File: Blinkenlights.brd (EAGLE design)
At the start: 33 x 44.5 mm, 15 parts, among them Q1 2N2222, Q2 2N2222

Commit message: 2.0.0913 Version updates
Minor modifications and tweaking
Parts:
- +, -: device adafruit:1X01 -> IXR:1X01-CLEANBIG
- Q1, Q2: device adafruit:TO92-EBC-OVAL -> IXR:TO92-EBC-OVAL
- U$1: device SparkFun:OSHW-LOGO-S -> IXR:OSHW-LOGO-S
- moved U$1 6.63 mm to (23.5, 36.2)
- moved LED2 1.42 mm to (26.7, 39.4)
- moved LED1 1.42 mm to (6.35, 39.4)
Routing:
- net N$6: track 14.9 -> 13.8 mm
- net N$5: track 14.9 -> 13.8 mm
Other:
- board text added: "BLINKENLIGHTS V2.0.0913"
- board text added: "CR2032 3V"
- board text added: "I LEARNED TO SOLDER!"
- board text removed: "BLINKENLIGHTS V2.0.0613"
- board text removed: "I Learned To Solder!"

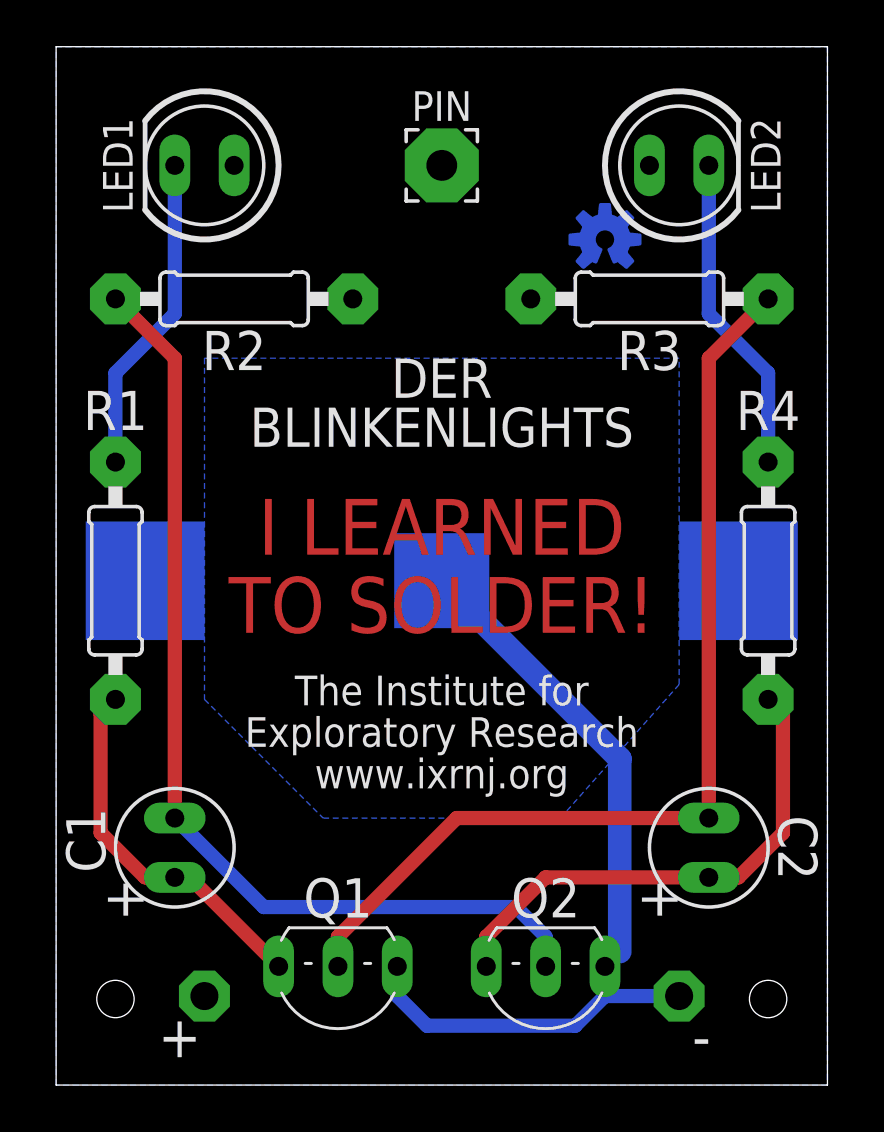
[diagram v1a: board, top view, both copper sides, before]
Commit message: v2.0.1401 Flipped battery clip - could not insert battery when lapel pin was installed.
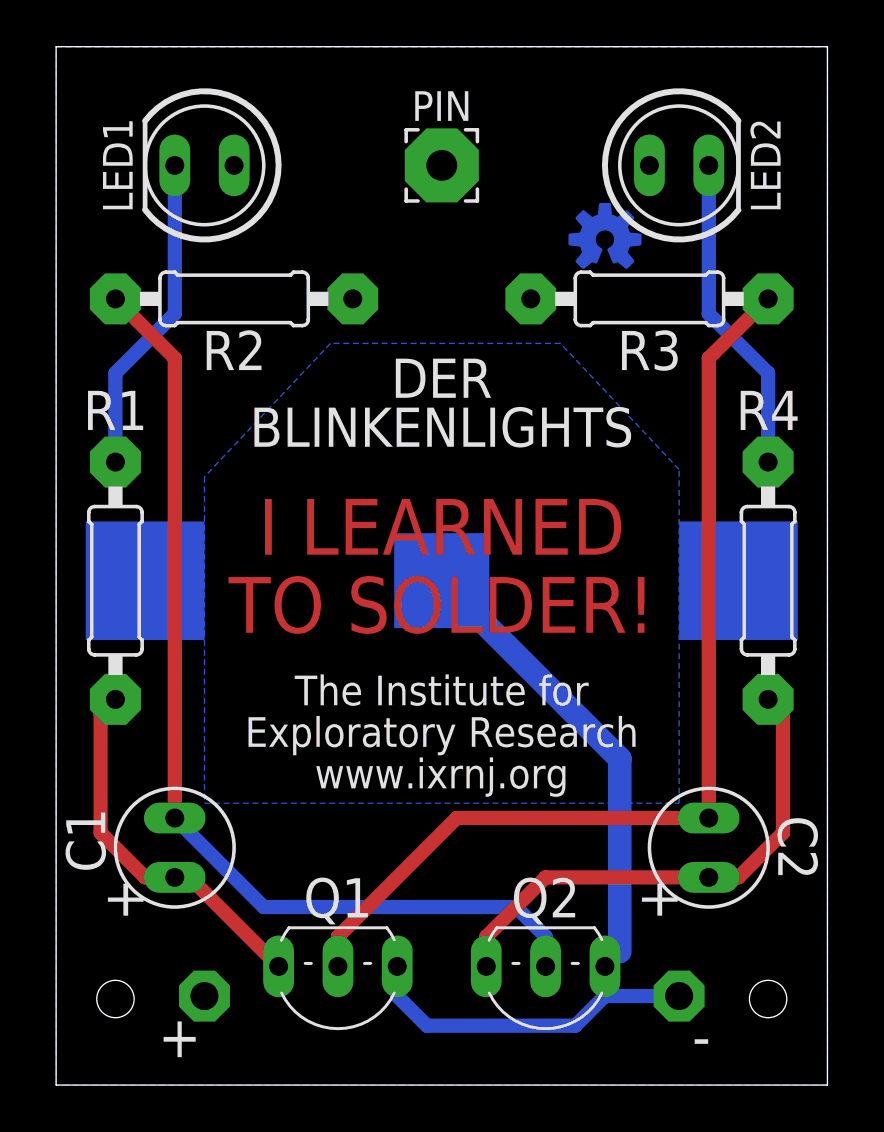
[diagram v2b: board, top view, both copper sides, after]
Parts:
- turned BATT to 180 degrees
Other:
- board text added: "BLINKENLIGHTS V2.0.1401"
- board text removed: "BLINKENLIGHTS V2.0.0913"
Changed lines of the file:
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@@
 <setting verticaltext="up"/>
 </settings>
-<grid distance="0.05" unitdist="inch" unit="inch" style="lines" multiple="1" display="yes" altdistance="0.0125" altunitdist="inch" altunit="inch"/>
+<grid distance="0.05" unitdist="inch" unit="inch" style="lines" multiple="1" display="yes" altdistance="0.0025" altunitdist="inch" altunit="inch"/>
 <layers>
 <layer number="1" name="Top" color="4" fill="1" visible="yes" active="yes"/>
@@
 <layer number="27" name="tValues" color="7" fill="1" visible="yes" active="yes"/>
 <layer number="28" name="bValues" color="7" fill="1" visible="no" active="yes"/>
-<layer number="29" name="tStop" color="7" fill="3" visible="yes" active="yes"/>
+<layer number="29" name="tStop" color="7" fill="3" visible="no" active="yes"/>
 <layer number="30" name="bStop" color="7" fill="6" visible="no" active="yes"/>
 <layer number="31" name="tCream" color="7" fill="4" visible="no" active="yes"/>
@@
 <hole x="2.54" y="3.683" drill="1.6"/>
 <hole x="30.48" y="3.683" drill="1.6"/>
-<text x="16.51" y="1.27" size="1.27" layer="26" font="vector" ratio="12" distance="0" rot="MR0" align="center">BLINKENLIGHTS V2.0.0913</text>
+<text x="16.51" y="1.27" size="1.27" layer="26" font="vector" ratio="12" distance="0" rot="MR0" align="center">BLINKENLIGHTS V2.0.1401</text>
 <text x="16.51" y="22.225" size="2.3876" layer="1" font="vector" ratio="18" distance="40" align="center">I LEARNED
 TO SOLDER!</text>
@@
 BLINKENLIGHTS</text>
 <text x="14.605" y="36.195" size="1.4224" layer="22" font="vector" ratio="12" rot="MR0" align="center">(CC) BY-SA</text>
-<text x="16.51" y="10.16" size="1.778" layer="22" font="vector" ratio="12" distance="0" rot="MR0" align="center">CR2032 3V</text>
+<text x="16.51" y="8.5725" size="1.778" layer="22" font="vector" ratio="12" distance="0" rot="MR0" align="center">CR2032 3V</text>
 <text x="16.51" y="22.225" size="2.3876" layer="29" font="vector" ratio="18" distance="40" align="center">I LEARNED
 TO SOLDER!</text>
+<wire x1="7.874" y1="34.29" x2="7.4295" y2="33.02" width="0.1524" layer="22"/>
+<wire x1="7.4295" y1="33.02" x2="6.985" y2="34.29" width="0.1524" layer="22"/>
+<wire x1="6.985" y1="34.29" x2="6.5405" y2="33.02" width="0.1524" layer="22"/>
+<wire x1="6.5405" y1="33.02" x2="6.096" y2="34.29" width="0.1524" layer="22"/>
+<wire x1="7.874" y1="34.29" x2="8.3185" y2="33.02" width="0.1524" layer="22"/>
+<wire x1="8.3185" y1="33.02" x2="8.763" y2="34.29" width="0.1524" layer="22"/>
+<wire x1="8.763" y1="34.29" x2="9.2075" y2="33.02" width="0.1524" layer="22"/>
+<wire x1="9.2075" y1="33.02" x2="9.4615" y2="33.655" width="0.1524" layer="22"/>
+<wire x1="9.4615" y1="33.655" x2="11.43" y2="33.655" width="0.1524" layer="22"/>
+<wire x1="6.096" y1="34.29" x2="5.842" y2="33.655" width="0.1524" layer="22"/>
+<wire x1="5.842" y1="33.655" x2="3.81" y2="33.655" width="0.1524" layer="22"/>
+<wire x1="25.654" y1="34.29" x2="25.2095" y2="33.02" width="0.1524" layer="22"/>
+<wire x1="25.2095" y1="33.02" x2="24.765" y2="34.29" width="0.1524" layer="22"/>
+<wire x1="24.765" y1="34.29" x2="24.3205" y2="33.02" width="0.1524" layer="22"/>
+<wire x1="24.3205" y1="33.02" x2="23.876" y2="34.29" width="0.1524" layer="22"/>
+<wire x1="25.654" y1="34.29" x2="26.0985" y2="33.02" width="0.1524" layer="22"/>
+<wire x1="26.0985" y1="33.02" x2="26.543" y2="34.29" width="0.1524" layer="22"/>
+<wire x1="26.543" y1="34.29" x2="26.9875" y2="33.02" width="0.1524" layer="22"/>
+<wire x1="26.9875" y1="33.02" x2="27.2415" y2="33.655" width="0.1524" layer="22"/>
+<wire x1="27.2415" y1="33.655" x2="29.21" y2="33.655" width="0.1524" layer="22"/>
+<wire x1="23.876" y1="34.29" x2="23.622" y2="33.655" width="0.1524" layer="22"/>
+<wire x1="23.622" y1="33.655" x2="21.59" y2="33.655" width="0.1524" layer="22"/>
 </plain>
 <attributes>
@@
 <attribute name="NAME" x="20.955" y="7.1755" size="1.6764" layer="25" font="vector" ratio="12" align="bottom-center"/>
 </element>
-<element name="BATT" library="adafruit" package="CR2032-SMD" value="CR2032" x="16.51" y="21.59" smashed="yes" rot="MR0">
-<attribute name="NAME" x="16.51" y="31.75" size="1.6764" layer="26" font="vector" ratio="12" rot="MR0" align="center"/>
+<element name="BATT" library="adafruit" package="CR2032-SMD" value="CR2032" x="16.51" y="21.59" smashed="yes" rot="MR180">
+<attribute name="NAME" x="16.51" y="11.1125" size="1.6764" layer="26" font="vector" ratio="12" rot="MR180" align="center"/>
 </element>
 <element name="R1" library="IXR" package="0207/10_BIG" value="220Ω" x="2.54" y="21.59" smashed="yes" rot="R90">
@@
 </signal>
 <signal name="N$7">
-<polygon width="0.4064" layer="16" pour="cutout">
-<vertex x="6.35" y="31.115"/>
-<vertex x="6.35" y="16.51"/>
-<vertex x="11.43" y="11.43"/>
-<vertex x="21.59" y="11.43"/>
-<vertex x="26.67" y="17.145"/>
-<vertex x="26.67" y="31.115"/>
+<polygon width="0.3048" layer="16" pour="cutout">
+<vertex x="11.7475" y="31.75"/>
+<vertex x="6.35" y="26.035"/>
+<vertex x="6.35" y="12.065"/>
+<vertex x="26.67" y="12.065"/>
+<vertex x="26.67" y="26.3525"/>
+<vertex x="21.59" y="31.75"/>
 </polygon>
 </signal>
